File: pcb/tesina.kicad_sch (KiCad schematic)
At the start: 12 parts, among them J1 Conn_01x02_Male, J5 AMP2_IN, J6 AMP3_IN, J7 AMP2_OUT, J8 AMP3_OUT

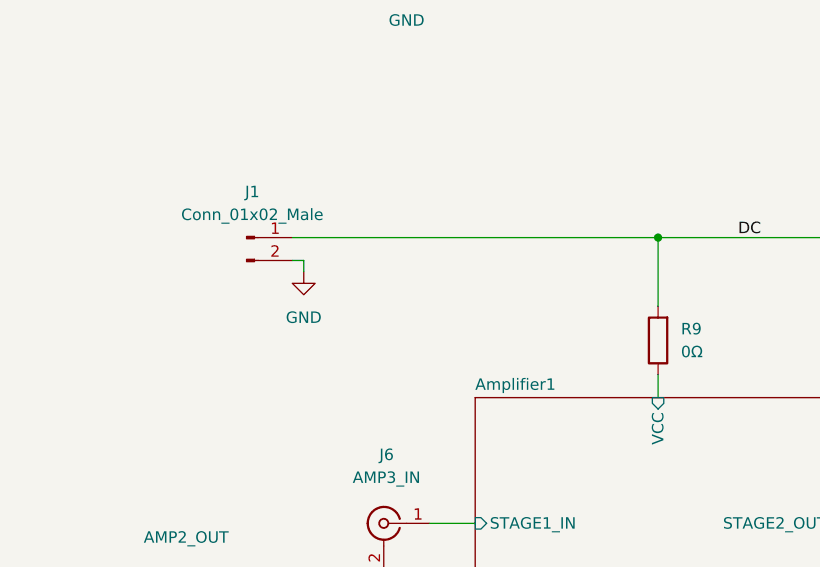
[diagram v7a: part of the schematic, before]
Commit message: alternate board
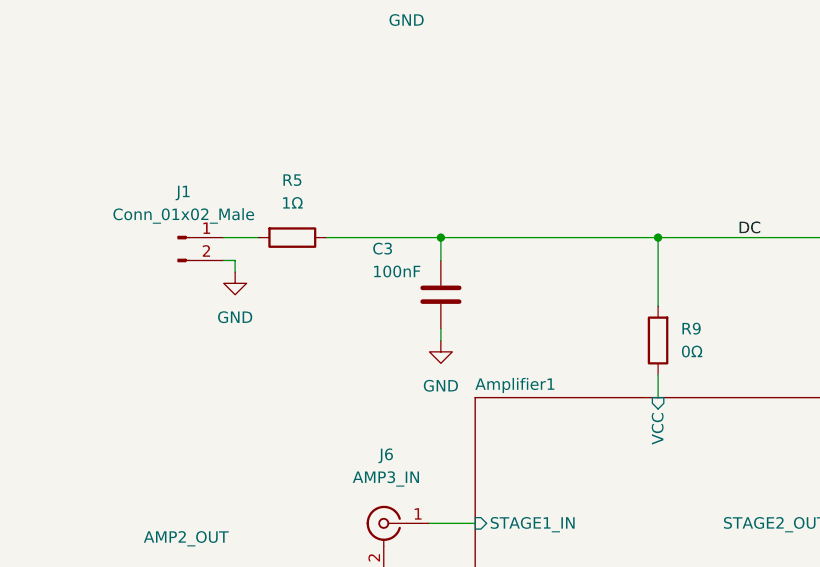
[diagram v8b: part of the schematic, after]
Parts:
- added C3: 100nF, Capacitor_SMD:C_1206_3216Metric, symbol Device:C
- added R5: 1Ω, Resistor_SMD:R_0603_1608Metric, symbol Device:R
- H1: footprint MountingHole:MountingHole_2.5mm_Pad_TopBottom -> MountingHole:MountingHole_2.7mm_M2.5_DIN965_Pad_TopBottom
- J1: footprint Connector_PinHeader_2.54mm:PinHeader_1x02_P2.54mm_Vertical -> Nicobigio01:Connector_Pad
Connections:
- net DC: now also C3.1, R5.1; no longer J1.1 (Pin_1)
- net GND: now also C3.2
- new net: J1.1 (Pin_1), R5.2
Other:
- moved on the sheet: J1
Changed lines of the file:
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@@
 (kicad_sch (version 20211123) (generator eeschema)
   (paper "A4")
+  (junction (at 128.27 82.55) (diameter 0) (color 0 0 0 0)
+  )
+  (junction (at 149.86 50.8) (diameter 0) (color 0 0 0 0)
+  )
   (junction (at 152.4 82.55) (diameter 0) (color 0 0 0 0)
   )
-  (junction (at 149.86 50.8) (diameter 0) (color 0 0 0 0)
-  )
   (junction (at 124.46 50.8) (diameter 0) (color 0 0 0 0)
   )
@@
   (junction (at 194.31 50.8) (diameter 0) (color 0 0 0 0)
   )
-  (wire (pts (xy 111.76 82.55) (xy 152.4 82.55))
+  (wire (pts (xy 104.14 82.55) (xy 107.95 82.55))
     (stroke (width 0) (type default) (color 0 0 0 0))
   )
@@
     (stroke (width 0) (type default) (color 0 0 0 0))
   )
+  (wire (pts (xy 128.27 82.55) (xy 128.27 85.09))
+    (stroke (width 0) (type default) (color 0 0 0 0))
+  )
+  (wire (pts (xy 115.57 82.55) (xy 128.27 82.55))
+    (stroke (width 0) (type default) (color 0 0 0 0))
+  )
   (wire (pts (xy 171.45 50.8) (xy 149.86 50.8))
     (stroke (width 0) (type default) (color 0 0 0 0))
@@
     (stroke (width 0) (type default) (color 0 0 0 0))
   )
+  (wire (pts (xy 128.27 92.71) (xy 128.27 93.98))
+    (stroke (width 0) (type default) (color 0 0 0 0))
+  )
   (wire (pts (xy 124.46 50.8) (xy 124.46 53.34))
     (stroke (width 0) (type default) (color 0 0 0 0))
@@
     (stroke (width 0) (type default) (color 0 0 0 0))
   )
-  (wire (pts (xy 113.03 85.09) (xy 113.03 86.36))
+  (wire (pts (xy 128.27 82.55) (xy 152.4 82.55))
+    (stroke (width 0) (type default) (color 0 0 0 0))
+  )
+  (wire (pts (xy 105.41 85.09) (xy 105.41 86.36))
     (stroke (width 0) (type default) (color 0 0 0 0))
   )
@@
     (stroke (width 0) (type default) (color 0 0 0 0))
   )
-  (wire (pts (xy 111.76 85.09) (xy 113.03 85.09))
+  (wire (pts (xy 104.14 85.09) (xy 105.41 85.09))
     (stroke (width 0) (type default) (color 0 0 0 0))
   )
@@
     )
     (pin "1")
+  )
+  (symbol (lib_id "Device:C") (at 128.27 88.9 0) (mirror y) (unit 1)
+    (in_bom yes) (on_board yes)
+    (property "Reference" "C3" (id 0) (at 120.65 83.82 0)
+      (effects (font (size 1.27 1.27)) (justify right))
+    )
+    (property "Value" "100nF" (id 1) (at 120.65 86.36 0)
+      (effects (font (size 1.27 1.27)) (justify right))
+    )
+    (property "Footprint" "Capacitor_SMD:C_1206_3216Metric" (id 2) (at 127.3048 92.71 0)
+      (effects (font (size 1.27 1.27)) hide)
+    )
+    (property "Datasheet" "~" (id 3) (at 128.27 88.9 0)
+      (effects (font (size 1.27 1.27)) hide)
+    )
+    (pin "1")
+    (pin "2")
   )
   (symbol (lib_id "Connector:Conn_Coaxial") (at 181.61 114.3 0) (unit 1)
@@
     (pin "1")
   )
-  (symbol (lib_id "power:GND") (at 113.03 86.36 0) (unit 1)
-    (in_bom yes) (on_board yes) (fields_autoplaced)
-    (property "Reference" "#PWR0110" (id 0) (at 113.03 92.71 0)
-      (effects (font (size 1.27 1.27)) hide)
-    )
-    (property "Value" "GND" (id 1) (at 113.03 91.44 0))
-    (property "Footprint" "" (id 2) (at 113.03 86.36 0)
-      (effects (font (size 1.27 1.27)) hide)
-    )
-    (property "Datasheet" "" (id 3) (at 113.03 86.36 0)
+  (symbol (lib_id "power:GND") (at 105.41 86.36 0) (unit 1)
+    (in_bom yes) (on_board yes) (fields_autoplaced)
+    (property "Reference" "#PWR0110" (id 0) (at 105.41 92.71 0)
+      (effects (font (size 1.27 1.27)) hide)
+    )
+    (property "Value" "GND" (id 1) (at 105.41 91.44 0))
+    (property "Footprint" "" (id 2) (at 105.41 86.36 0)
+      (effects (font (size 1.27 1.27)) hide)
+    )
+    (property "Datasheet" "" (id 3) (at 105.41 86.36 0)
       (effects (font (size 1.27 1.27)) hide)
     )
@@
       (effects (font (size 1.27 1.27)) (justify left))
     )
-    (property "Footprint" "MountingHole:MountingHole_2.5mm_Pad_TopBottom" (id 2) (at 124.46 44.45 0)
+    (property "Footprint" "MountingHole:MountingHole_2.7mm_M2.5_DIN965_Pad_TopBottom" (id 2) (at 124.46 44.45 0)
       (effects (font (size 1.27 1.27)) hide)
     )
     (property "Datasheet" "~" (id 3) (at 124.46 44.45 0)
+      (effects (font (size 1.27 1.27)) hide)
+    )
+    (pin "1")
+  )
+  (symbol (lib_id "power:GND") (at 128.27 93.98 0) (unit 1)
+    (in_bom yes) (on_board yes) (fields_autoplaced)
+    (property "Reference" "#PWR0102" (id 0) (at 128.27 100.33 0)
+      (effects (font (size 1.27 1.27)) hide)
+    )
+    (property "Value" "GND" (id 1) (at 128.27 99.06 0))
+    (property "Footprint" "" (id 2) (at 128.27 93.98 0)
+      (effects (font (size 1.27 1.27)) hide)
+    )
+    (property "Datasheet" "" (id 3) (at 128.27 93.98 0)
       (effects (font (size 1.27 1.27)) hide)
     )
@@
     )
     (pin "1")
+  )
+  (symbol (lib_id "Device:R") (at 111.76 82.55 270) (unit 1)
+    (in_bom yes) (on_board yes) (fields_autoplaced)
+    (property "Reference" "R5" (id 0) (at 111.76 76.2 90))
+    (property "Value" "1Ω" (id 1) (at 111.76 78.74 90))
+    (property "Footprint" "Resistor_SMD:R_0603_1608Metric" (id 2) (at 111.76 80.772 90)
+      (effects (font (size 1.27 1.27)) hide)
+    )
+    (property "Datasheet" "~" (id 3) (at 111.76 82.55 0)
+      (effects (font (size 1.27 1.27)) hide)
+    )
+    (pin "1")
+    (pin "2")
   )
   (symbol (lib_id "Connector:Conn_Coaxial") (at 121.92 114.3 0) (mirror y) (unit 1)
@@
     (pin "2")
   )
-  (symbol (lib_id "Connector:Conn_01x02_Male") (at 106.68 82.55 0) (unit 1)
+  (symbol (lib_id "Connector:Conn_01x02_Male") (at 99.06 82.55 0) (unit 1)
     (in_bom yes) (on_board yes)
-    (property "Reference" "J1" (id 0) (at 107.315 77.47 0))
-    (property "Value" "Conn_01x02_Male" (id 1) (at 107.315 80.01 0))
-    (property "Footprint" "Connector_PinHeader_2.54mm:PinHeader_1x02_P2.54mm_Vertical" (id 2) (at 106.68 82.55 0)
-      (effects (font (size 1.27 1.27)) hide)
-    )
-    (property "Datasheet" "~" (id 3) (at 106.68 82.55 0)
+    (property "Reference" "J1" (id 0) (at 99.695 77.47 0))
+    (property "Value" "Conn_01x02_Male" (id 1) (at 99.695 80.01 0))
+    (property "Footprint" "Nicobigio01:Connector_Pad" (id 2) (at 99.06 82.55 0)
+      (effects (font (size 1.27 1.27)) hide)
+    )
+    (property "Datasheet" "~" (id 3) (at 99.06 82.55 0)
       (effects (font (size 1.27 1.27)) hide)
     )
@@
       (reference "#PWR0101") (unit 1) (value "GND") (footprint "")
     )
-    (path "/87ee7424-77dd-42bb-9d0a-6365445b897a/a598646c-3518-4d91-99b2-48db8ed13230"
+    (path "/c62d96f2-d66b-45b6-a4d1-776f8f074eb2"
       (reference "#PWR0102") (unit 1) (value "GND") (footprint "")
     )
@@
       (reference "#PWR0110") (unit 1) (value "GND") (footprint "")
     )
+    (path "/87ee7424-77dd-42bb-9d0a-6365445b897a/782bde9f-eaf3-4cdd-8f09-56315be975db"
+      (reference "#PWR0111") (unit 1) (value "GND") (footprint "")
+    )
     (path "/a5d88b64-c3d9-4f91-bd07-74a2502d5d70"
       (reference "#PWR0122") (unit 1) (value "GND") (footprint "")
@@
       (reference "#PWR0129") (unit 1) (value "GND") (footprint "")
     )
-    (path "/87ee7424-77dd-42bb-9d0a-6365445b897a/f10d4adb-f024-4c05-ad2a-4fe8bc51b34a"
-      (reference "#PWR?") (unit 1) (value "GND") (footprint "")
-    )
     (path "/87ee7424-77dd-42bb-9d0a-6365445b897a/ac03c825-4c12-4c29-b388-30701e68b944"
       (reference "C1") (unit 1) (value "100pF") (footprint "Capacitor_SMD:C_0603_1608Metric")
@@
       (reference "C2") (unit 1) (value "100pF") (footprint "Capacitor_SMD:C_0603_1608Metric")
     )
-    (path "/87ee7424-77dd-42bb-9d0a-6365445b897a/bf454069-d31b-45f3-bb19-88b39d3d1c27"
-      (reference "C3") (unit 1) (value "100pF") (footprint "Capacitor_SMD:C_0603_1608Metric")
+    (path "/2dead8c7-406d-48fe-937b-fa955a19f275"
+      (reference "C3") (unit 1) (value "100nF") (footprint "Capacitor_SMD:C_1206_3216Metric")
     )
     (path "/87ee7424-77dd-42bb-9d0a-6365445b897a/1dc0307f-3744-4b2d-a94b-0dfce7235a0a"
@@
       (reference "C5") (unit 1) (value "100pF") (footprint "Capacitor_SMD:C_0603_1608Metric")
     )
+    (path "/87ee7424-77dd-42bb-9d0a-6365445b897a/97aca013-487d-4c23-b562-8346b39024f2"
+      (reference "C6") (unit 1) (value "100pF") (footprint "Capacitor_SMD:C_0603_1608Metric")
+    )
     (path "/4e3d076a-abc7-4ccc-a891-541b92d429fd/d4ea7fa6-1841-4de9-ba37-7965ae7c1256"
       (reference "C7") (unit 1) (value "100pF") (footprint "Capacitor_SMD:C_0603_1608Metric")
@@
       (reference "C20") (unit 1) (value "100pF") (footprint "Capacitor_SMD:C_0603_1608Metric")
     )
-    (path "/87ee7424-77dd-42bb-9d0a-6365445b897a/0493fad5-de27-4ec6-ac8b-c4dfccc03df1"
-      (reference "C?") (unit 1) (value "100nF") (footprint "Capacitor_SMD:C_1206_3216Metric")
-    )
     (path "/b5a1e2cf-8653-43c2-a55c-ab49b56c5509"
-      (reference "H1") (unit 1) (value "MountingHole_Pad") (footprint "MountingHole:MountingHole_2.5mm_Pad_TopBottom")
+      (reference "H1") (unit 1) (value "MountingHole_Pad") (footprint "MountingHole:MountingHole_2.7mm_M2.5_DIN965_Pad_TopBottom")
     )
     (path "/90789f7a-49b9-44f5-ab0b-28086fbe0ff7"
@@
     )
     (path "/eadf55f3-20fd-4e1c-86b3-87abe0b9b698"
-      (reference "J1") (unit 1) (value "Conn_01x02_Male") (footprint "Connector_PinHeader_2.54mm:PinHeader_1x02_P2.54mm_Vertical")
+      (reference "J1") (unit 1) (value "Conn_01x02_Male") (footprint "Nicobigio01:Connector_Pad")
     )
     (path "/61f8178c-bdb9-4f9f-bd8f-70114bf6ae6d"
@@
       (reference "R4") (unit 1) (value "375Ω") (footprint "Resistor_SMD:R_0603_1608Metric")
     )
+    (path "/d9149a36-b5bc-4ddd-bcad-7a18287f8435"
+      (reference "R5") (unit 1) (value "1Ω") (footprint "Resistor_SMD:R_0603_1608Metric")
+    )
     (path "/ce8e496d-c502-4b6a-b31c-1f1c9765bc9e"
